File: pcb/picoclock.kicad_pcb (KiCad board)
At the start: 2 copper layers, 175.8 x 64 mm, 85 parts, among them J1 UART, J10 USB, J11 Alt Power, J12 PWM, J13 AUDIO, J15 Conn_01x24, J2 AUDIO, J3 xx, J4 xx, J5 Micro_SD_Card_Det1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

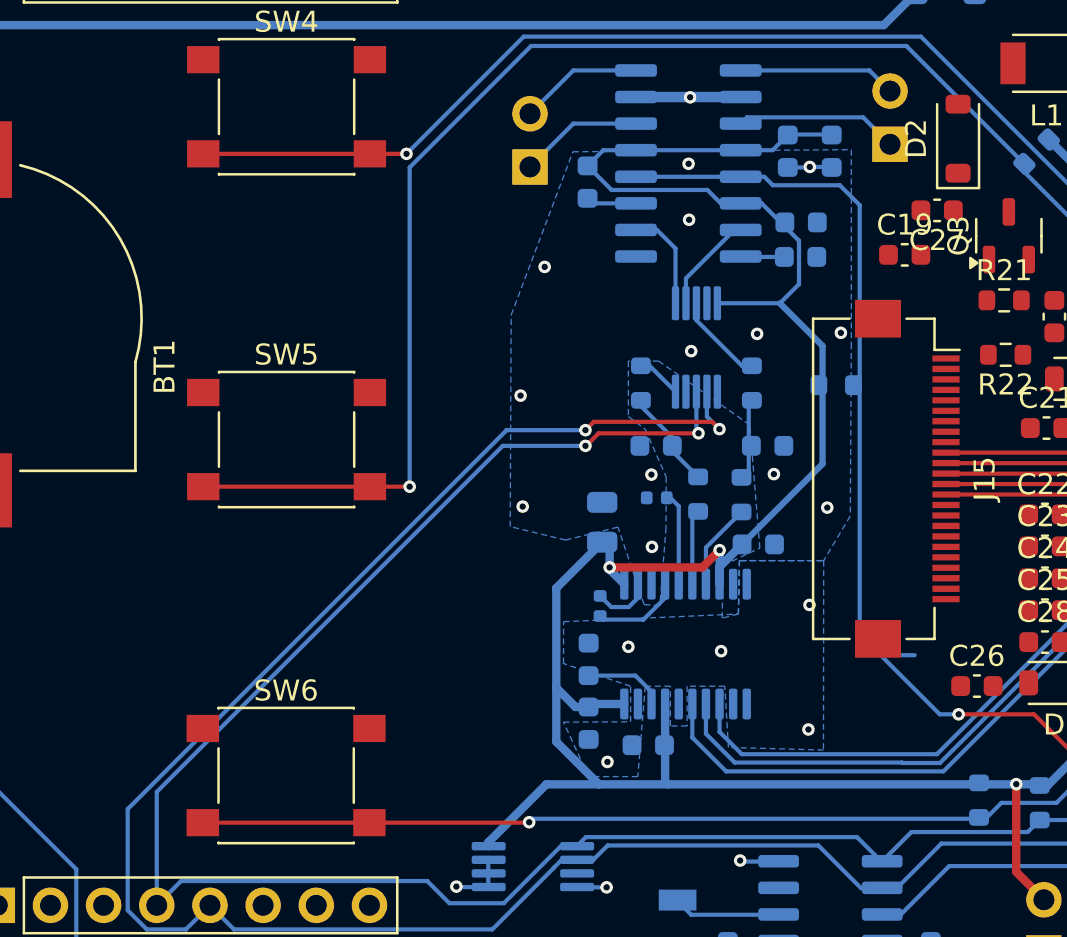
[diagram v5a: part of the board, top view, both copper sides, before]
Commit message: [pcb] audio circuit fixes
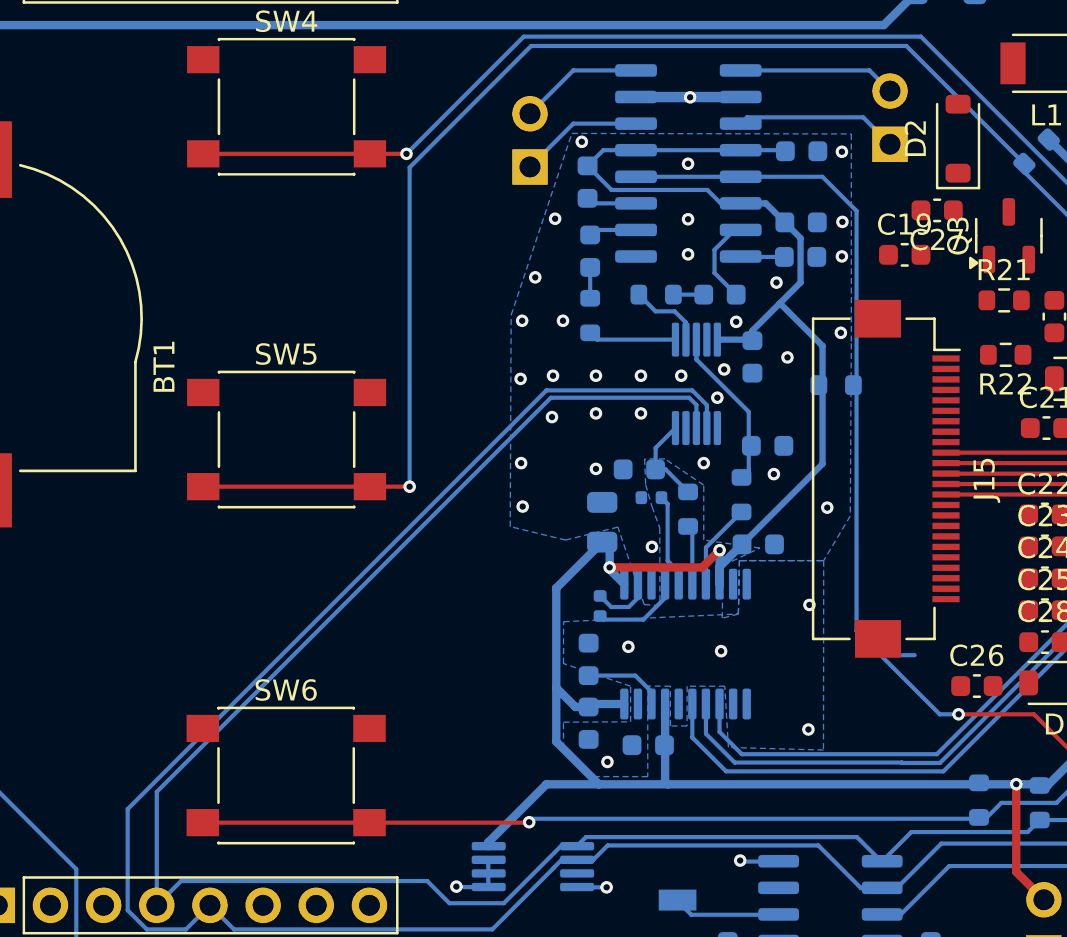
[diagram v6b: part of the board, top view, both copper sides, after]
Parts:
- added C18: 4.7uF, Capacitor_SMD:C_0603_1608Metric, B.Cu at (120.2, 91.9)
- added C29: 4.7uF, Capacitor_SMD:C_0603_1608Metric, B.Cu at (114.0, 89.8)
- moved C15 10.5 mm to (121.8, 94.9)
- moved R15 6.23 mm to (117.2, 91.9), turned to 180 degrees
- moved R14 4.04 mm to (114.0, 92.9), turned to 90 degrees
- moved U7 1.74 mm to (119.1, 96.2)
- moved C10 1.38 mm to (116.4, 100.3)
- moved R2 0.86 mm to (118.7, 102.2)
- moved C16 0.66 mm to (124.1, 85.1), turned to 0 degrees
- moved C8 0.26 mm to (117.0, 101.6)
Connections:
- R14 pad 1: Net-(U7-P1B) -> Net-(U7-P1W)
- R14 pad 2: LINE_OUT_LEFT -> Net-(C29-Pad1)
- R15 pad 1: LINE_OUT_RIGHT -> Net-(C18-Pad1)
- R15 pad 2: Net-(U7-P0B) -> Net-(U7-P0W)
- U7 pad 5: Net-(U7-P1B) -> LINE_OUT_LEFT
- U7 pad 6: LOR_ADJ -> Net-(U7-P1W)
- U7 pad 7: LOL_ADJ -> Net-(U7-P0W)
- U7 pad 8: Net-(U7-P0B) -> LINE_OUT_RIGHT
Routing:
- net Net-(U7-P0B): track 4.36 -> 0.00 mm
- net Net-(U7-P1W): track 0.00 -> 4.21 mm
- net LINE_OUT_RIGHT: track 3.89 -> 7.76 mm
- net Net-(U7-P0W): track 0.00 -> 3.62 mm
- net LOR_ADJ: track 4.87 -> 2.29 mm
- net Net-(U7-P1B): track 2.16 -> 0.00 mm
- net GND: track 38.7 -> 36.6 mm, vias 29 -> 48
- net Net-(C29-Pad1): track 0.00 -> 1.47 mm
- net Net-(C18-Pad1): track 0.00 -> 1.45 mm
- net +3.3V: track 303.7 -> 302.4 mm
- net LOL_ADJ: track 5.13 -> 4.21 mm
- net SCL: track 111.0 -> 110.2 mm, vias 2 -> 0
- net Net-(U4-OUTL): track 3.59 -> 2.84 mm
- net SDA: track 103.8 -> 103.7 mm, vias 3 -> 1

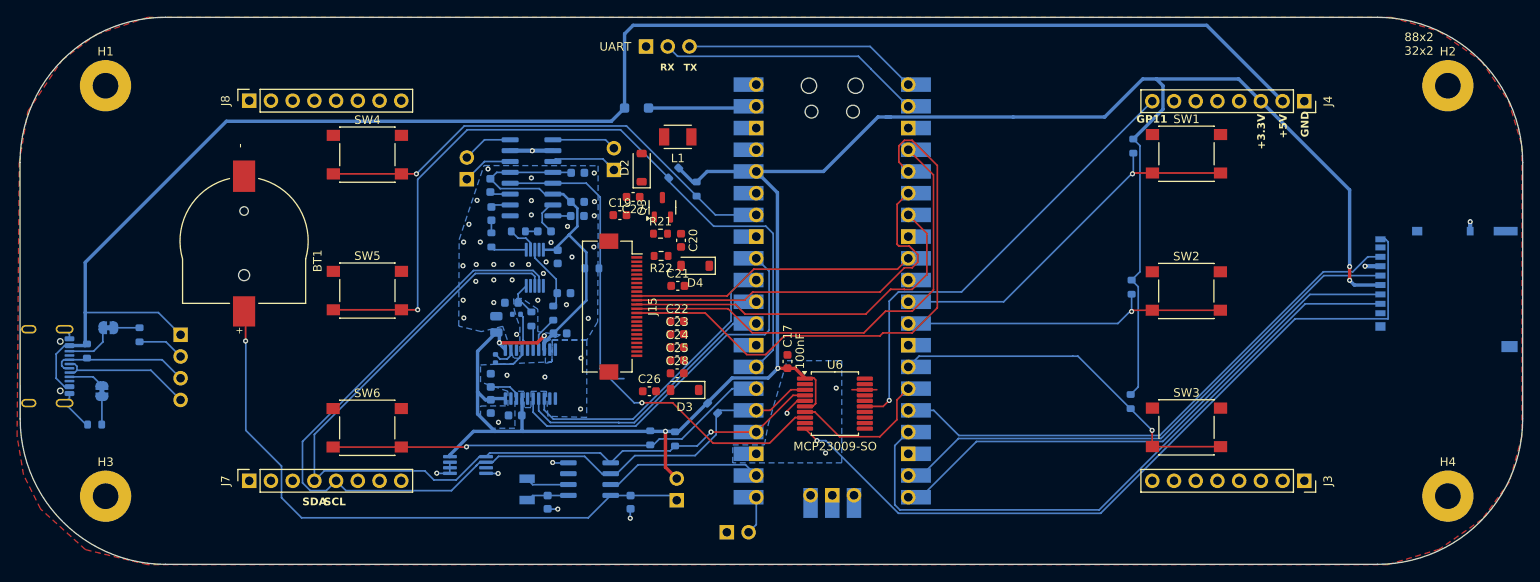
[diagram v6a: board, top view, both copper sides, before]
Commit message: [pcb] fpc screen connector at the right place
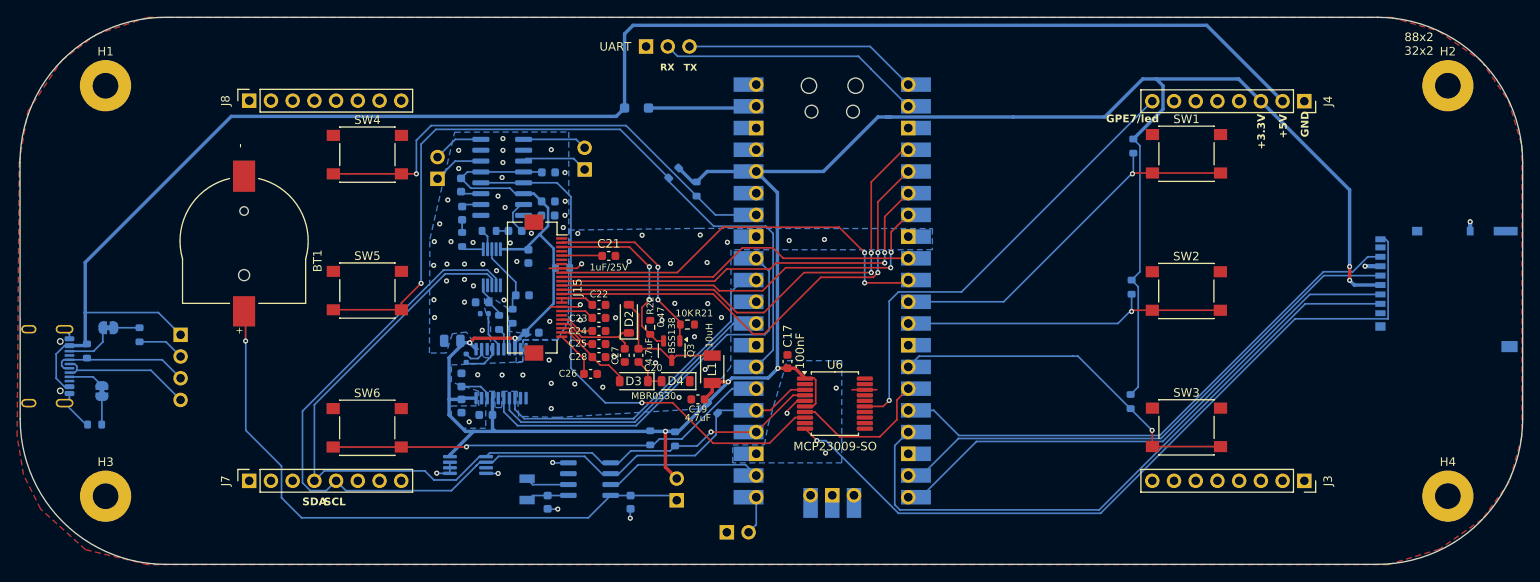
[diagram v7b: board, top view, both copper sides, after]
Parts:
- moved L1 27.5 mm to (139.8, 108.0), turned to 90 degrees
- moved C19 23.4 mm to (138.2, 111.6), turned to 180 degrees
- moved C27 18.6 mm to (129.6, 106.4), turned to -90 degrees
- moved D2 17.7 mm to (130.1, 102.2)
- moved Q3 16.8 mm to (135.1, 105.9), turned to -90 degrees
- moved C20 14.3 mm to (131.2, 106.4)
- moved D4 13.7 mm to (135.6, 109.5)
- moved R21 11.1 mm to (136.9, 102.8)
- moved C23 9.35 mm to (126.6, 102.0)
- moved C25 9.35 mm to (126.6, 105.1)
- moved C28 9.35 mm to (126.6, 106.6)
- moved C22 9.35 mm to (126.6, 100.5)
- moved C24 9.35 mm to (126.6, 103.6)
- moved J15 9.05 mm to (120.4, 98.5)
- moved C21 8.80 mm to (127.8, 94.8)
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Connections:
- net GPIO/led renamed GPE7/led
- U6 pad 9: SHDN -> unconnected-(U6-GP1-Pad9)
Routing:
- net GPIO5 SCREEN BUSY: track 0.00 -> 47.7 mm, vias 0 -> 2
- net GDR: track 0.00 -> 22.3 mm, vias 0 -> 2
- net RESE: track 0.00 -> 21.8 mm, vias 0 -> 2
- net Net-(D2-A): track 0.00 -> 15.0 mm
- net VGH: track 0.00 -> 10.4 mm
- net GPIO3 SPI0 TX: track 67.1 -> 56.9 mm, vias 0 -> 2
- net VGL: track 0.00 -> 9.55 mm
- net GPIO1 SCREEN RST: track 33.6 -> 42.4 mm
- net Net-(J15-Pin_24): track 0.00 -> 5.58 mm
- net Net-(J15-Pin_5): track 0.00 -> 4.75 mm
- net +3.3V: track 302.4 -> 306.8 mm, vias 6 -> 7
- net Net-(J15-Pin_15): track 0.00 -> 4.40 mm
- net Net-(J15-Pin_22): track 0.00 -> 4.34 mm
- net Net-(D3-K): track 0.00 -> 4.31 mm
- net Net-(J15-Pin_20): track 0.00 -> 4.12 mm
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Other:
- board text added: "GPE7/led"
- board text removed: "GP11"

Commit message: [pcb] fixes for mcp23009 (bad footprint)
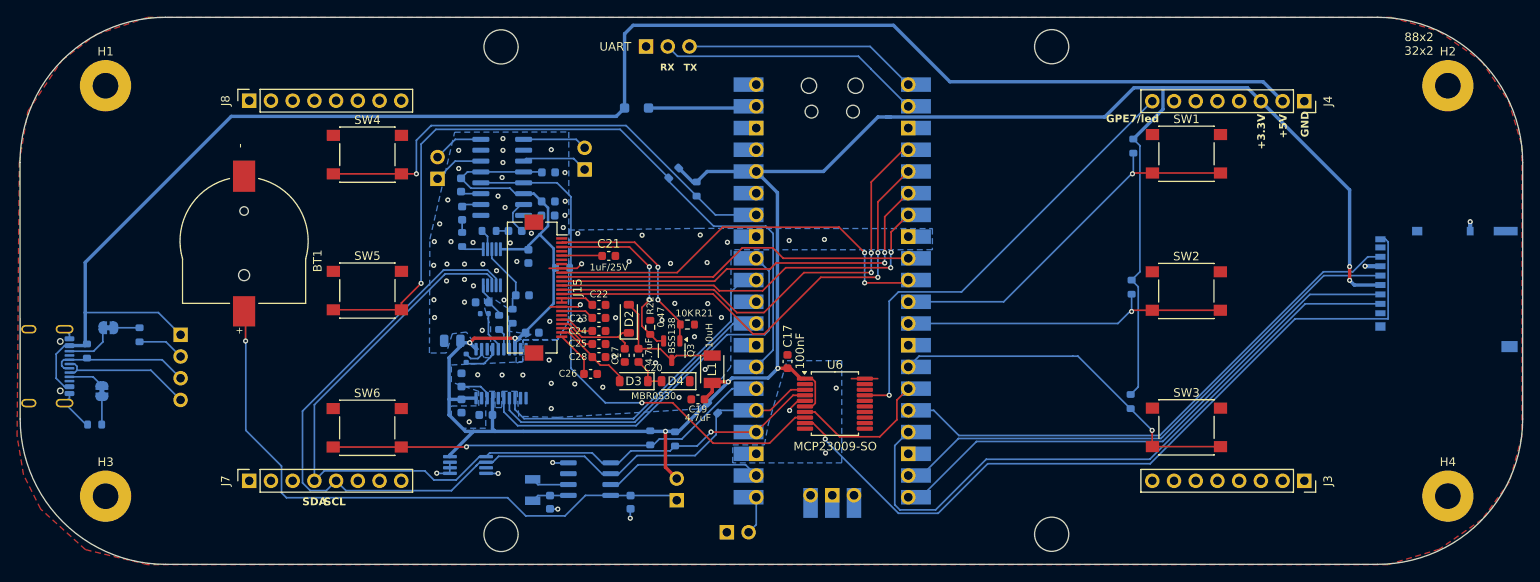
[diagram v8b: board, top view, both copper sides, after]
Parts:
- moved Y1 0.65 mm to (118.8, 122.2)
- moved C1 0.28 mm to (120.9, 123.6)
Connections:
- U6 pad 10: SD_DET -> unconnected-(U6-NC-Pad10)_1
- U6 pad 15: GPE7/led -> unconnected-(U6-GP5-Pad15)
- U6 pad 16: (no net) -> unconnected-(U6-GP6-Pad16)
- U6 pad 17: (no net) -> GPE7/led
- U6 pad 18: GND -> unconnected-(U6-NC-Pad10)_3
- U6 pad 19: (no net) -> unconnected-(U6-NC-Pad10)_2
- U6 pad 2: (no net) -> unconnected-(U6-NC-Pad10)
- U6 pad 20: (no net) -> GND
- U6 pad 9: unconnected-(U6-GP1-Pad9) -> SD_DET
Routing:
- net +3.3V: track 306.8 -> 304.4 mm
- net GPE7/led: track 55.2 -> 54.3 mm
- net GND: track 39.3 -> 38.6 mm
- net Net-(U1-OSCI): track 5.00 -> 4.39 mm
- net Net-(U1-OSCO): track 5.18 -> 4.57 mm
- net SD_DET: track 91.7 -> 92.3 mm
- net 3V BATT: track 72.2 -> 71.7 mm
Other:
- outline, holes or cut-outs redrawn
